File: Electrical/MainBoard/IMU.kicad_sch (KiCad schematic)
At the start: 4 parts, among them U6 ICM-42688-P

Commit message: Begin layout of pcb
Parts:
- renumbered U6 to U4

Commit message: Add some finishing touches and create preliminary boms
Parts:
- C2: value 10 nF -> 0.01 uF
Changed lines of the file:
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@@
       (effects (font (size 1.27 1.27)) (justify left))
     )
-    (property "Value" "10 nF" (at 83.82 137.16 0)
+    (property "Value" "0.01 uF" (at 83.82 137.16 0)
       (effects (font (size 1.27 1.27)) (justify left))
     )

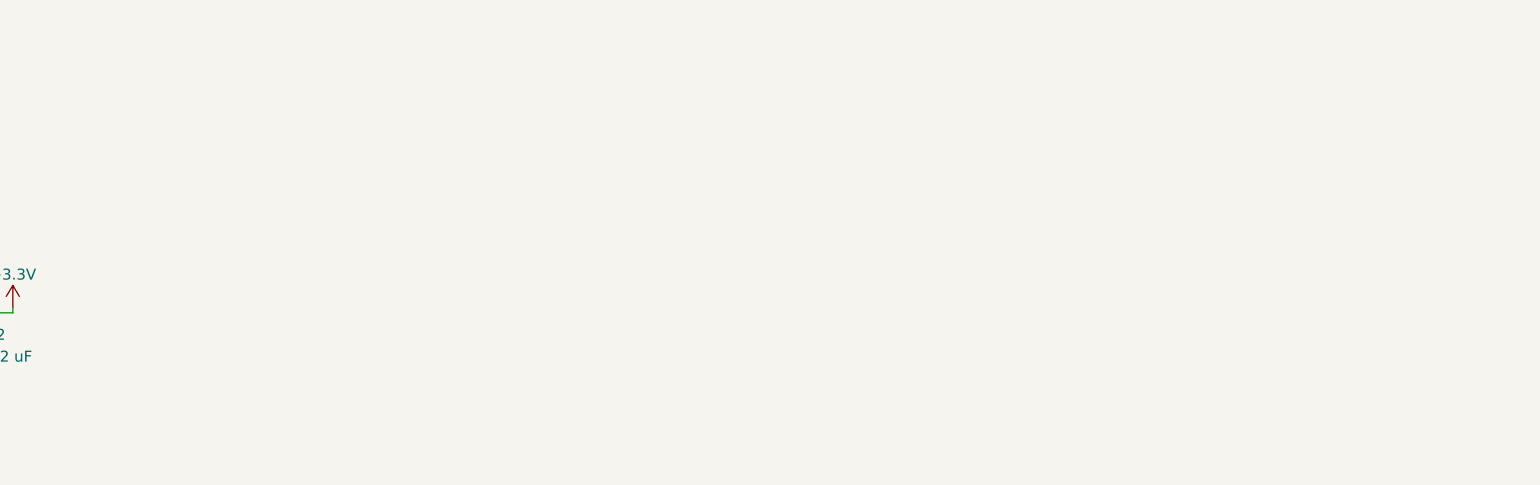
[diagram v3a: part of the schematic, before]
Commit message: Add comments to schematic for future revs
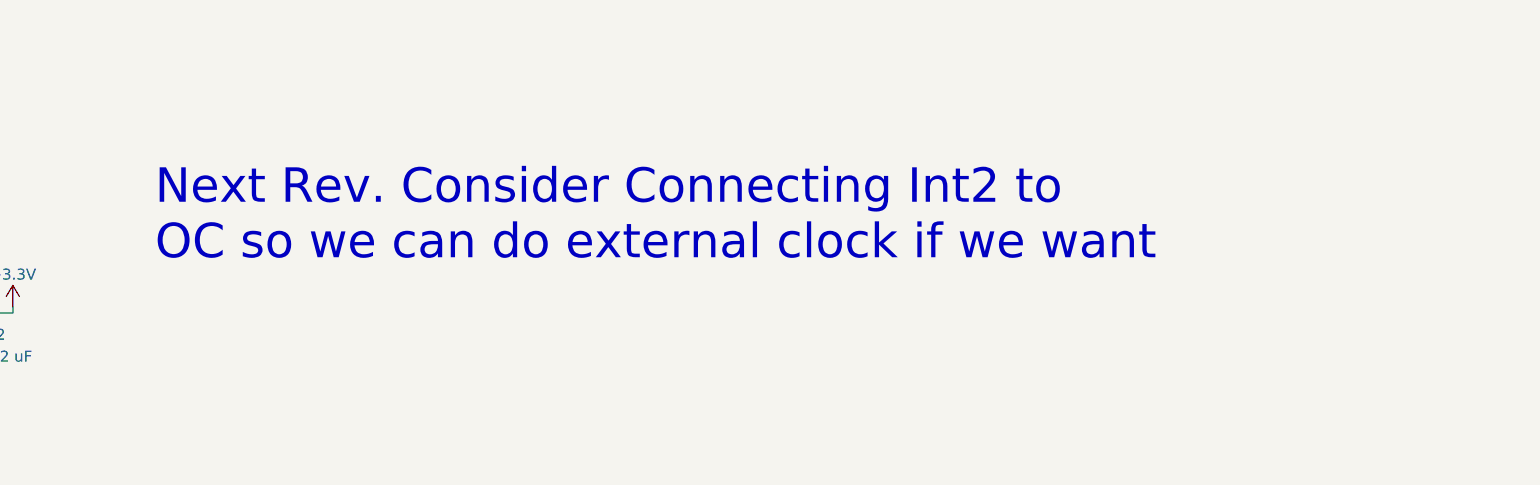
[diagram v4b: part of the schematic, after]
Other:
- note added: "Next Rev. Consider Connecting Int2 to OC so we can do external clock if we want"
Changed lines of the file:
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@@
     (effects (font (size 3 3)) (justify left bottom))
+  )
+  (text "Next Rev. Consider Connecting Int2 to \nOC so we can do external clock if we want"
+    (at 209.55 131.445 0)
+    (effects (font (size 4 4)) (justify left bottom))
   )
   (hierarchical_label "SDO1" (shape input) (at 175.26 121.92 0) (fields_autoplaced)

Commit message: Made V0.2 revisions to Main Board
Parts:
- added J26: Conn_02x04_Odd_Even, Connector_PinHeader_2.54mm:PinHeader_2x04_P2.54mm_Vertical, symbol Connector_Generic:Conn_02x04_Odd_Even
- C2, U4: now not fitted; now left out of the parts list
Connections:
- net +3.3V: now also J26.1 (Pin_1)
- net GND: now also J26.2 (Pin_2)
- net IMU_INT1: now also J26.5 (Pin_5)
- net IMU_INT2: now also J26.3 (Pin_3)
- net SCK1: now also J26.4 (Pin_4)
- net SDI1: now also J26.8 (Pin_8)
- net SDO1: now also J26.7 (Pin_7)
- net SS1*: now also J26.6 (Pin_6)
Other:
- note removed: "Next Rev. Consider Connecting Int2 to OC so we can do external clock if we want"
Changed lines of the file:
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@@
   (title_block
     (title "MCU Controller")
-    (rev "0.1")
+    (rev "0.2")
     (company "satomm@stanford.edu")
     (comment 1 "Department of Civil and Environmental Engineering")
@@
     (stroke (width 0) (type default))
   )
+  (wire (pts (xy 138.43 166.37) (xy 126.365 166.37))
+    (stroke (width 0) (type default))
+  )
   (wire (pts (xy 108.585 137.16) (xy 111.76 137.16))
     (stroke (width 0) (type default))
@@
   )
   (wire (pts (xy 175.26 129.54) (xy 175.26 130.81))
+    (stroke (width 0) (type default))
+  )
+  (wire (pts (xy 105.41 166.37) (xy 113.665 166.37))
     (stroke (width 0) (type default))
   )
@@
     (effects (font (size 3 3)) (justify left bottom))
   )
-  (text "Next Rev. Consider Connecting Int2 to \nOC so we can do external clock if we want"
-    (at 209.55 131.445 0)
-    (effects (font (size 4 4)) (justify left bottom))
-  )
   (hierarchical_label "SDO1" (shape input) (at 175.26 121.92 0) (fields_autoplaced)
     (effects (font (size 1.27 1.27)) (justify left))
+  )
+  (hierarchical_label "SDO1" (shape input) (at 113.665 173.99 180) (fields_autoplaced)
+    (effects (font (size 1.27 1.27)) (justify right))
   )
   (hierarchical_label "SDI1" (shape output) (at 111.125 121.92 180) (fields_autoplaced)
     (effects (font (size 1.27 1.27)) (justify right))
   )
+  (hierarchical_label "IMU_INT2" (shape output) (at 113.665 168.91 180) (fields_autoplaced)
+    (effects (font (size 1.27 1.27)) (justify right))
+  )
+  (hierarchical_label "IMU_INT1" (shape output) (at 113.665 171.45 180) (fields_autoplaced)
+    (effects (font (size 1.27 1.27)) (justify right))
+  )
   (hierarchical_label "SS1*" (shape input) (at 175.26 127 0) (fields_autoplaced)
     (effects (font (size 1.27 1.27)) (justify left))
@@
     (effects (font (size 1.27 1.27)) (justify left))
   )
+  (hierarchical_label "SS1*" (shape input) (at 126.365 171.45 0) (fields_autoplaced)
+    (effects (font (size 1.27 1.27)) (justify left))
+  )
   (hierarchical_label "SCK1" (shape input) (at 175.26 124.46 0) (fields_autoplaced)
     (effects (font (size 1.27 1.27)) (justify left))
   )
+  (hierarchical_label "SCK1" (shape input) (at 126.365 168.91 0) (fields_autoplaced)
+    (effects (font (size 1.27 1.27)) (justify left))
+  )
   (hierarchical_label "3V3" (shape input) (at 160.655 179.07 0) (fields_autoplaced)
+    (effects (font (size 1.27 1.27)) (justify left))
+  )
+  (hierarchical_label "SDI1" (shape output) (at 126.365 173.99 0) (fields_autoplaced)
     (effects (font (size 1.27 1.27)) (justify left))
   )
@@
     )
   )
+  (symbol (lib_id "Connector_Generic:Conn_02x04_Odd_Even") (at 118.745 168.91 0) (unit 1)
+    (in_bom yes) (on_board yes) (dnp no) (fields_autoplaced)
+    (property "Reference" "J26" (at 120.015 160.02 0)
+      (effects (font (size 1.27 1.27)))
+    )
+    (property "Value" "Conn_02x04_Odd_Even" (at 120.015 162.56 0)
+      (effects (font (size 1.27 1.27)))
+    )
+    (property "Footprint" "Connector_PinHeader_2.54mm:PinHeader_2x04_P2.54mm_Vertical" (at 118.745 168.91 0)
+      (effects (font (size 1.27 1.27)) hide)
+    )
+    (property "Datasheet" "~" (at 118.745 168.91 0)
+      (effects (font (size 1.27 1.27)) hide)
+    )
+    (pin "1")
+    (pin "2")
+    (pin "3")
+    (pin "4")
+    (pin "5")
+    (pin "6")
+    (pin "7")
+    (pin "8")
+    (instances
+      (project "MainBoard"
+        (path "/bd24c4db-4e36-4117-bd4f-5228ef241da9/d4596efc-cbfe-411a-9b03-58f747019e1a"
+          (reference "J26") (unit 1)
+        )
+      )
+    )
+  )
   (symbol (lib_id "power:+3.3V") (at 156.845 177.165 0) (unit 1)
     (in_bom yes) (on_board yes) (dnp no)
@@
   )
   (symbol (lib_id "Device:C") (at 177.8 140.97 0) (unit 1)
-    (in_bom yes) (on_board yes) (dnp no)
+    (in_bom no) (on_board no) (dnp yes)
     (property "Reference" "C2" (at 170.815 139.7 0)
       (effects (font (size 1.27 1.27)) (justify left))
@@
       (effects (font (size 1.27 1.27)) hide)
     )
+    (property "Sim.Enable" "0" (at 177.8 140.97 0)
+      (effects (font (size 1.27 1.27)) hide)
+    )
     (pin "1")
     (pin "2")
@@
   )
   (symbol (lib_id "Device:C") (at 186.69 140.97 0) (unit 1)
-    (in_bom yes) (on_board yes) (dnp no)
+    (in_bom no) (on_board no) (dnp yes)
     (property "Reference" "C2" (at 189.865 139.7 0)
       (effects (font (size 1.27 1.27)) (justify left))
@@
     )
     (property "Supplier 2 P/N" "" (at 186.69 140.97 0)
+      (effects (font (size 1.27 1.27)) hide)
+    )
+    (property "Sim.Enable" "0" (at 186.69 140.97 0)
       (effects (font (size 1.27 1.27)) hide)
     )
@@
   )
   (symbol (lib_id "Device:C") (at 92.71 135.89 0) (unit 1)
-    (in_bom yes) (on_board yes) (dnp no)
+    (in_bom no) (on_board no) (dnp yes)
     (property "Reference" "C2" (at 85.725 134.62 0)
       (effects (font (size 1.27 1.27)) (justify left))
@@
     )
     (property "Supplier 2 P/N" "" (at 92.71 135.89 0)
+      (effects (font (size 1.27 1.27)) hide)
+    )
+    (property "Sim.Enable" "0" (at 92.71 135.89 0)
       (effects (font (size 1.27 1.27)) hide)
     )
@@
   )
   (symbol (lib_id "RobotLibary:ICM-42688-P") (at 111.76 121.92 0) (unit 1)
-    (in_bom yes) (on_board yes) (dnp no)
+    (in_bom no) (on_board no) (dnp yes)
     (property "Reference" "U4" (at 142.875 114.3 0)
       (effects (font (size 3 3)))
@@
     )
     (property "Supplier 2 P/N" "" (at 111.76 121.92 0)
+      (effects (font (size 1.27 1.27)) hide)
+    )
+    (property "Sim.Enable" "0" (at 111.76 121.92 0)
       (effects (font (size 1.27 1.27)) hide)
     )
@@
     )
   )
+  (symbol (lib_id "power:GND") (at 138.43 166.37 0) (unit 1)
+    (in_bom yes) (on_board yes) (dnp no) (fields_autoplaced)
+    (property "Reference" "#PWR026" (at 138.43 172.72 0)
+      (effects (font (size 1.27 1.27)) hide)
+    )
+    (property "Value" "GND" (at 138.43 171.45 0)
+      (effects (font (size 1.27 1.27)))
+    )
+    (property "Footprint" "" (at 138.43 166.37 0)
+      (effects (font (size 1.27 1.27)) hide)
+    )
+    (property "Datasheet" "" (at 138.43 166.37 0)
+      (effects (font (size 1.27 1.27)) hide)
+    )
+    (pin "1")
+    (instances
+      (project "MainBoard"
+        (path "/bd24c4db-4e36-4117-bd4f-5228ef241da9"
+          (reference "#PWR026") (unit 1)
+        )
+        (path "/bd24c4db-4e36-4117-bd4f-5228ef241da9/d4596efc-cbfe-411a-9b03-58f747019e1a"
+          (reference "#PWR0165") (unit 1)
+        )
+      )
+    )
+  )
   (symbol (lib_id "power:GND") (at 108.585 139.7 0) (unit 1)
     (in_bom yes) (on_board yes) (dnp no) (fields_autoplaced)
@@
         )
       )
+    )
+  )
+  (symbol (lib_id "power:+3.3V") (at 105.41 166.37 0) (unit 1)
+    (in_bom yes) (on_board yes) (dnp no)
+    (property "Reference" "#PWR025" (at 105.41 170.18 0)
+      (effects (font (size 1.27 1.27)) hide)
+    )
+    (property "Value" "+3.3V" (at 105.41 162.56 0)
+      (effects (font (size 1.27 1.27)))
+    )
+    (property "Footprint" "" (at 105.41 166.37 0)
+      (effects (font (size 1.27 1.27)) hide)
+    )
+    (property "Datasheet" "" (at 105.41 166.37 0)
+      (effects (font (size 1.27 1.27)) hide)
+    )
+    (pin "1")
+    (instances
+      (project "MainBoard"
+        (path "/bd24c4db-4e36-4117-bd4f-5228ef241da9"
+          (reference "#PWR025") (unit 1)
+        )
+        (path "/bd24c4db-4e36-4117-bd4f-5228ef241da9/d4596efc-cbfe-411a-9b03-58f747019e1a"
+          (reference "#PWR081") (unit 1)
+        )
+      )

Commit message: Finalize rev 0.2
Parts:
- J26: Supplier 1 (none) -> DigiKey; Supplier 1 P/N (none) -> 10129381-908001BLF-ND
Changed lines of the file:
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@@
+      (effects (font (size 1.27 1.27)) hide)
+    )
+    (property "Description" "" (at 118.745 168.91 0)
+      (effects (font (size 1.27 1.27)) hide)
+    )
+    (property "Mfr" "" (at 118.745 168.91 0)
+      (effects (font (size 1.27 1.27)) hide)
+    )
+    (property "Mfr P/N" "" (at 118.745 168.91 0)
+      (effects (font (size 1.27 1.27)) hide)
+    )
+    (property "Supplier 1" "DigiKey" (at 118.745 168.91 0)
+      (effects (font (size 1.27 1.27)) hide)
+    )
+    (property "Supplier 1 P/N" "10129381-908001BLF-ND" (at 118.745 168.91 0)
+      (effects (font (size 1.27 1.27)) hide)
+    )
+    (property "Supplier 2" "" (at 118.745 168.91 0)
+      (effects (font (size 1.27 1.27)) hide)
+    )
+    (property "Supplier 2 P/N" "" (at 118.745 168.91 0)
       (effects (font (size 1.27 1.27)) hide)
     )

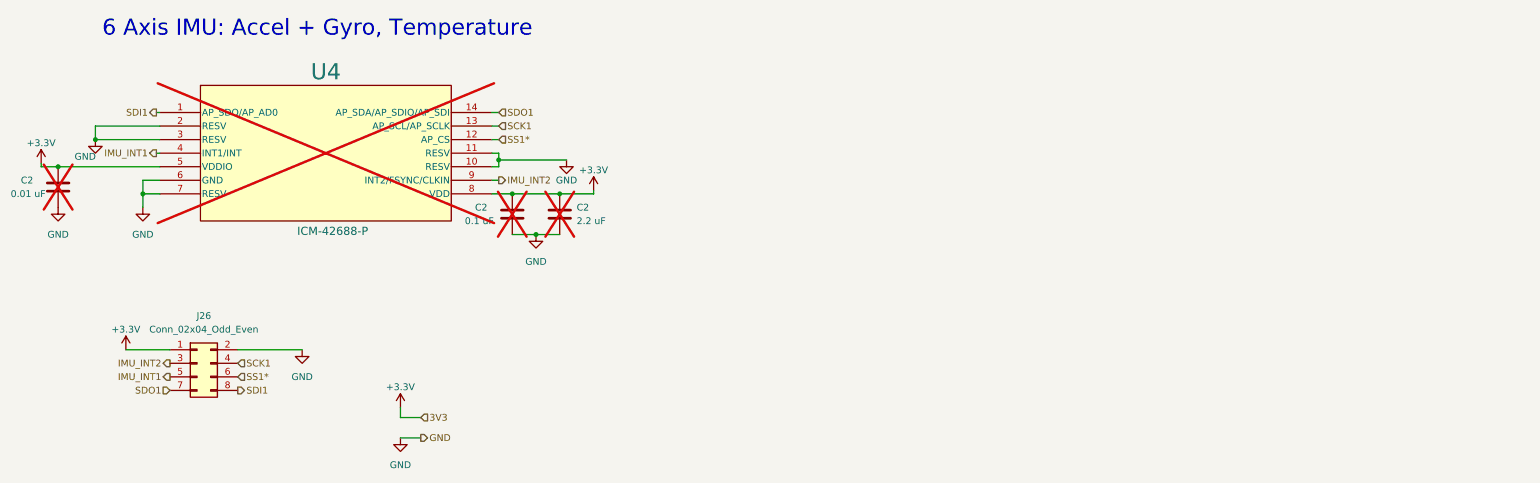
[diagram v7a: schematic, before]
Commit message: Fix SPI3 and make visual improvements
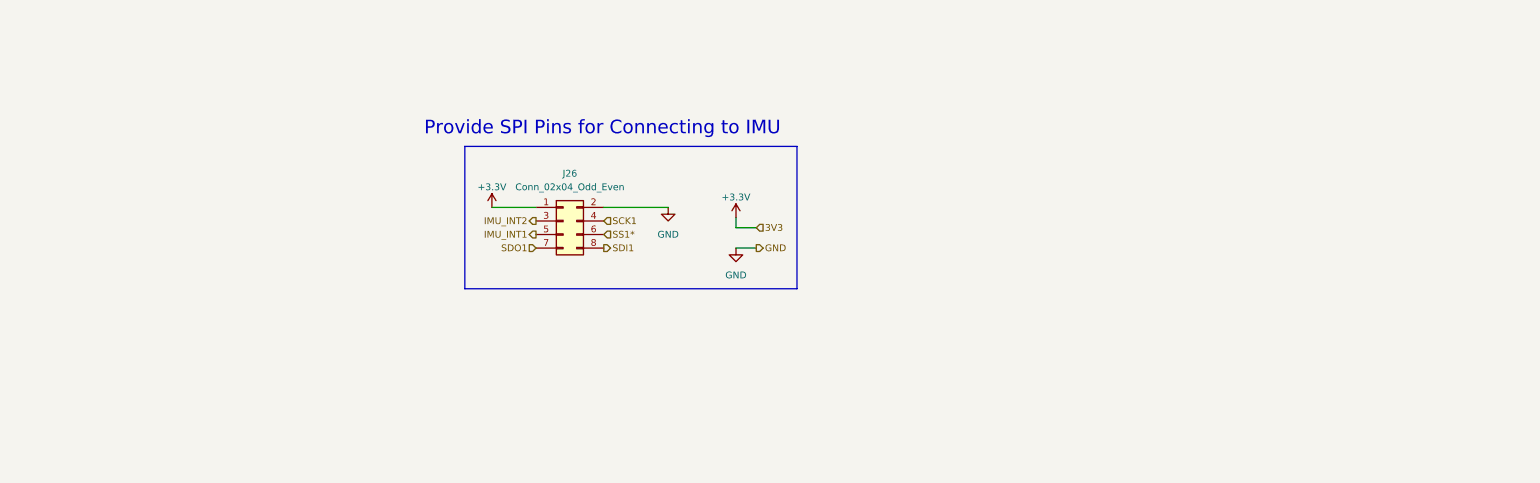
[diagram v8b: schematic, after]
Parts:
- removed C2: 0.1 uF, Capacitor_SMD:C_0805_2012Metric_Pad1.18x1.45mm_HandSolder, symbol Device:C
- removed C2: 2.2 uF, Capacitor_SMD:C_0805_2012Metric_Pad1.18x1.45mm_HandSolder, symbol Device:C
- removed C2: 0.01 uF, Capacitor_SMD:C_0805_2012Metric_Pad1.18x1.45mm_HandSolder, symbol Device:C
- removed U4: ICM-42688-P, RobotLibrary:LGA14_2P5X3X0P91_TDK-M, symbol RobotLibary:ICM-42688-P
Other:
- note added: "Provide SPI Pins for Connecting to IMU"
- note removed: "6 Axis IMU: Accel + Gyro, Temperature"
- moved on the sheet: J26
